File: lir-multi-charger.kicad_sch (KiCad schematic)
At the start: 45 parts, among them J1 USB_C_Receptacle_USB2.0, J2 Conn_01x02_Male, J3 Conn_01x02_Male, J4 Conn_01x02_Male, J5 Conn_01x02_Male, J6 Conn_01x02_Male, J7 Screw_Terminal_01x02, J8 Conn_01x02_Pin, U1 CN3130, U2 CN3130, U3 CN3130

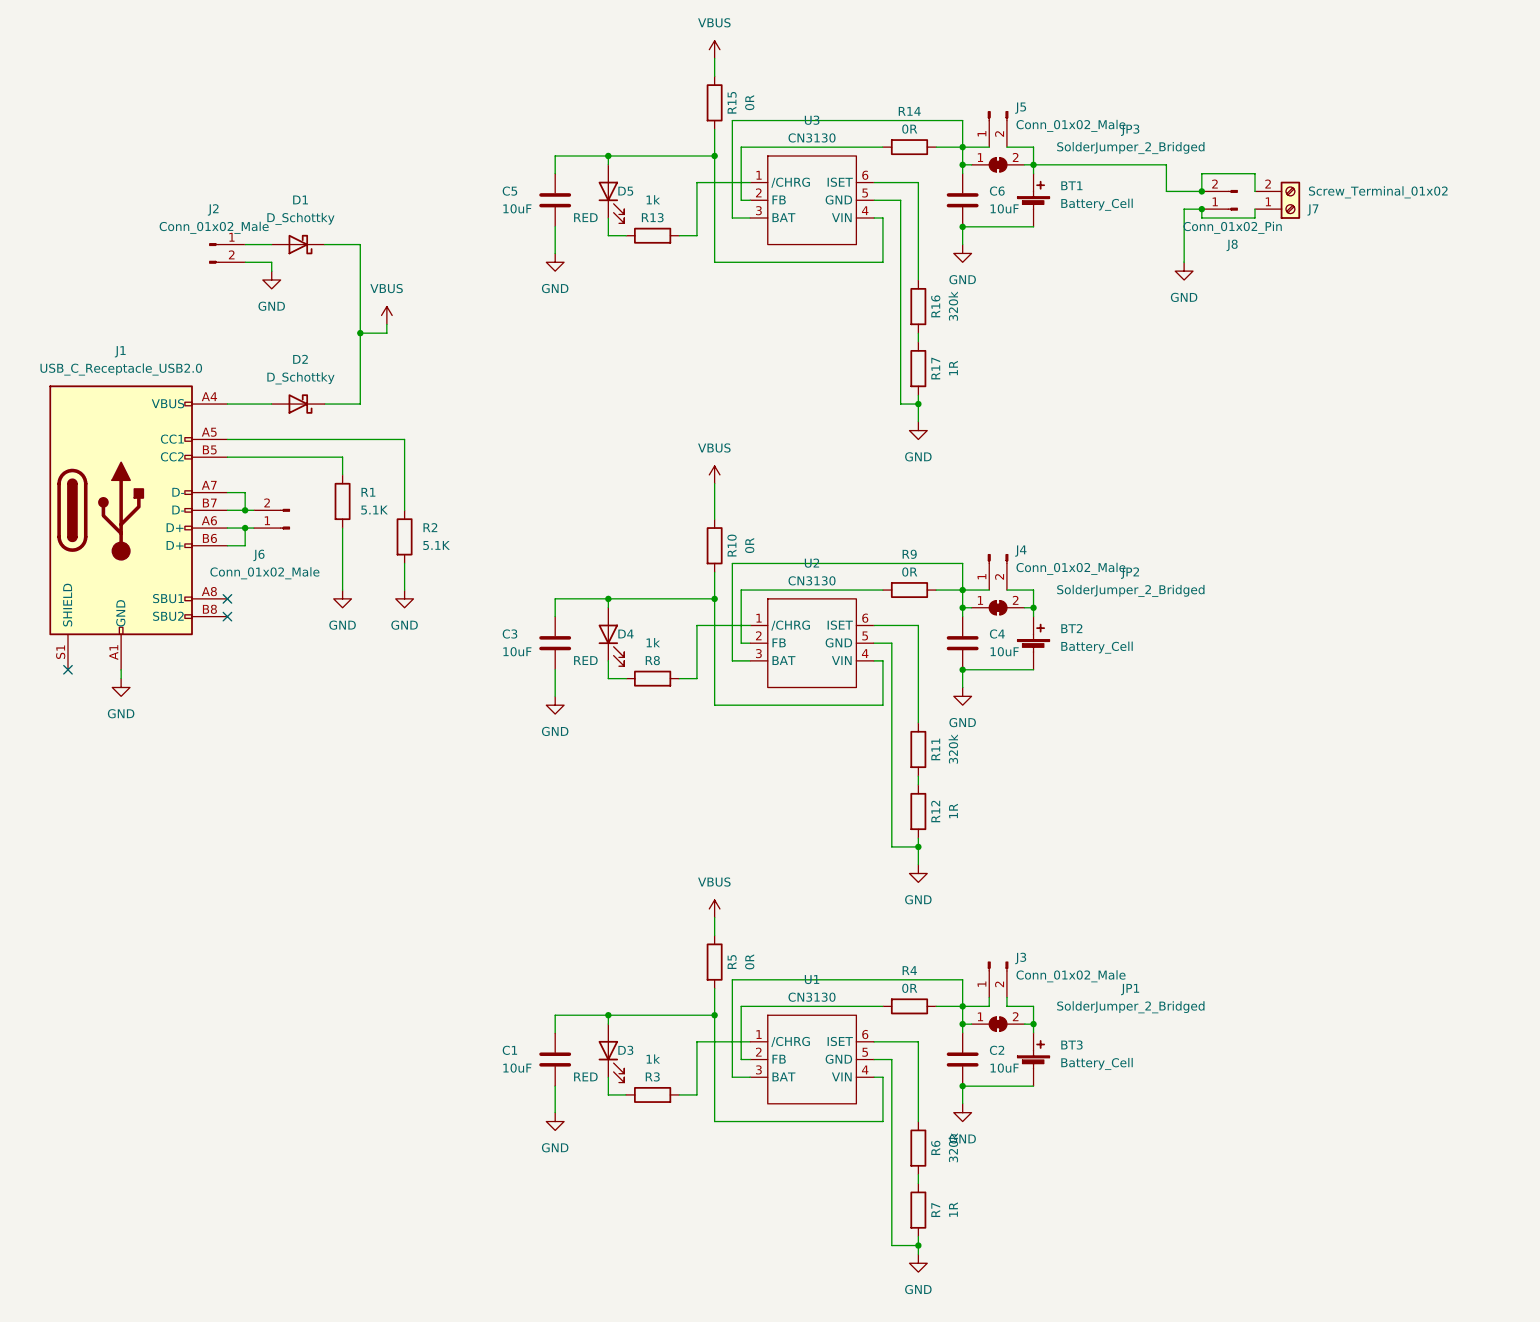
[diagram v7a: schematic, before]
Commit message: Revert "upgraded kicad version to 9, starting to add ext bat connectors"
This reverts commit a6eeaf41d868e39ea5ead22df93e0c5d5fe9c91a.
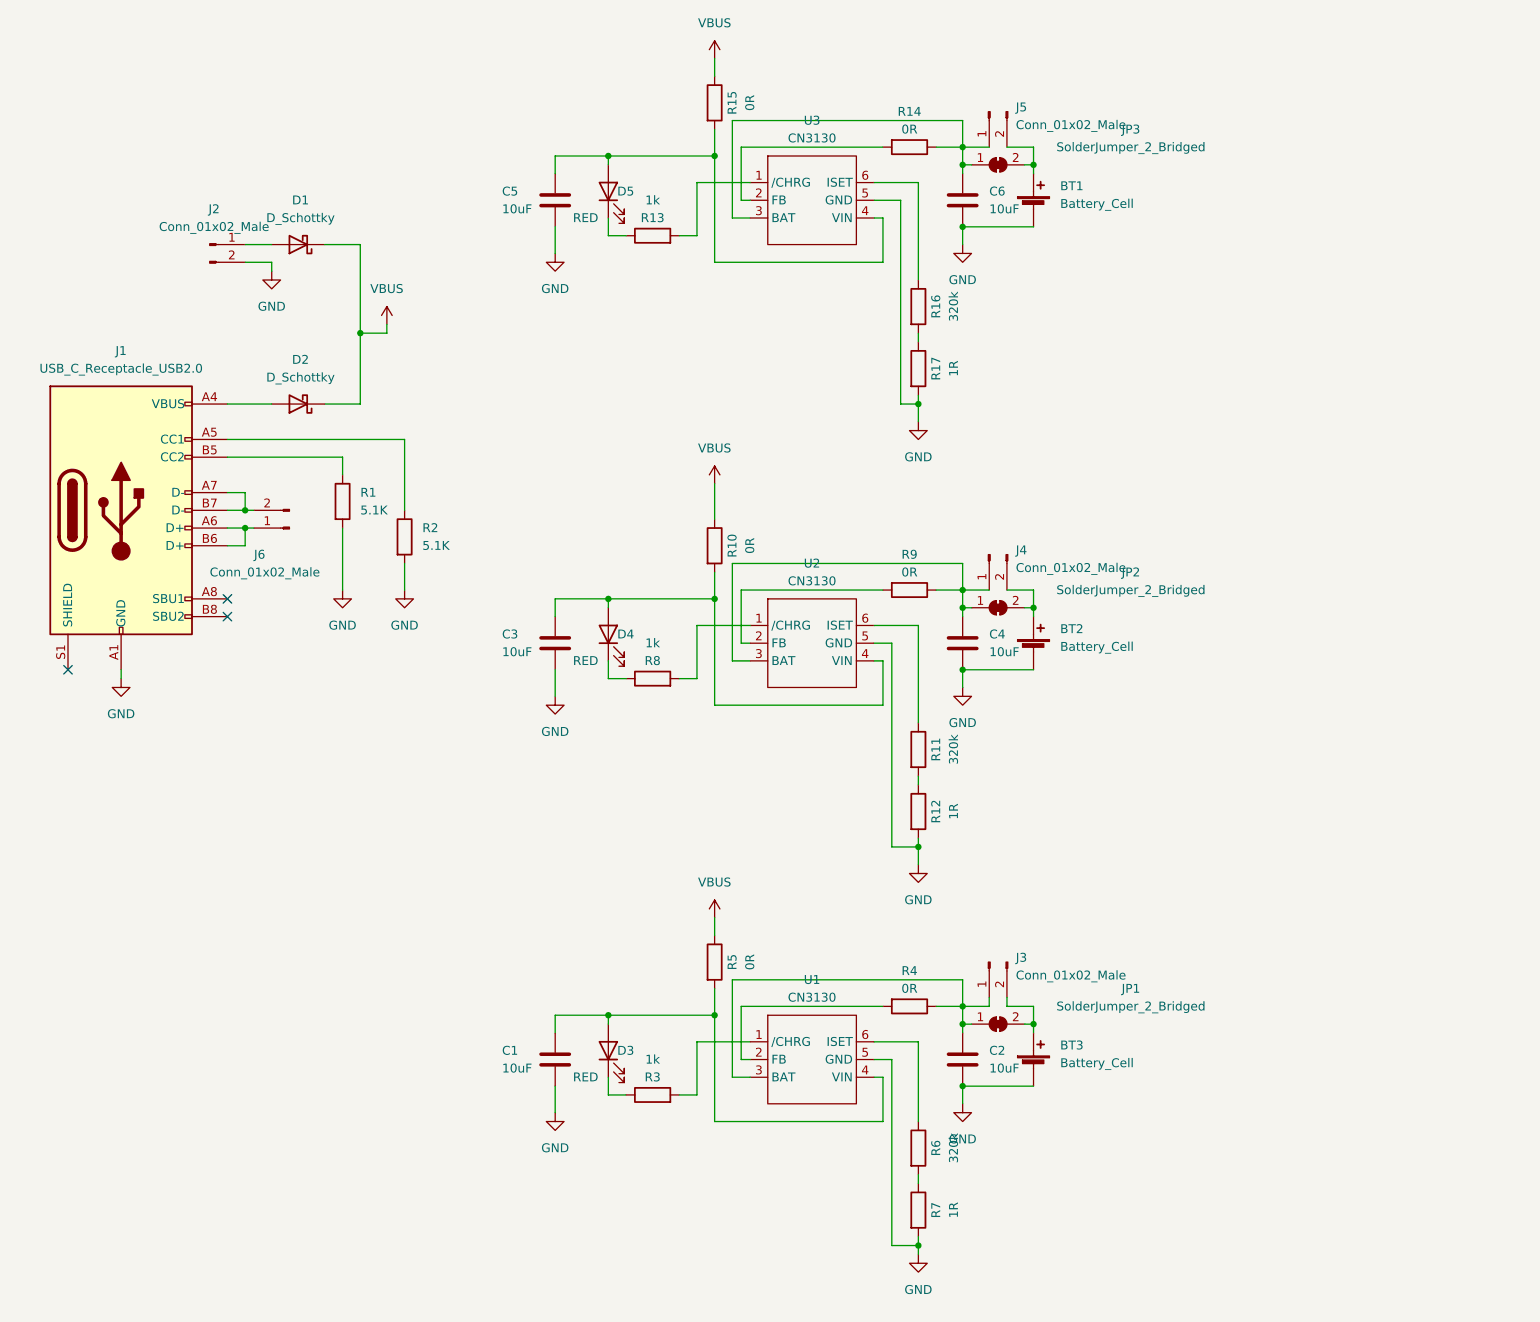
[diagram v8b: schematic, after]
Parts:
- removed J7: Screw_Terminal_01x02, TerminalBlock_4Ucon:TerminalBlock_4Ucon_1x02_P3.50mm_Horizontal, symbol Connector:Screw_Terminal_01x02
- removed J8: Conn_01x02_Pin, Connector_PinHeader_2.54mm:PinHeader_1x02_P2.54mm_Vertical, symbol Connector:Conn_01x02_Pin
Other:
- title: LIR-MULTI-CHARGER -> (none)
